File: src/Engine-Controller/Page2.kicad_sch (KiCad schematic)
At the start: 35 parts, among them P2 282837-6, P4 Micro_SD_Card, P5 USB, P6 140-504-415-000, P9 54602-908LF, Q1 QS5U17TR, U11 TS391IYLT, U4 SST25VF040B-50-4I-S2AE-T, U5 CP2102-GMR(QFN28), U7 SN65HVD71DR

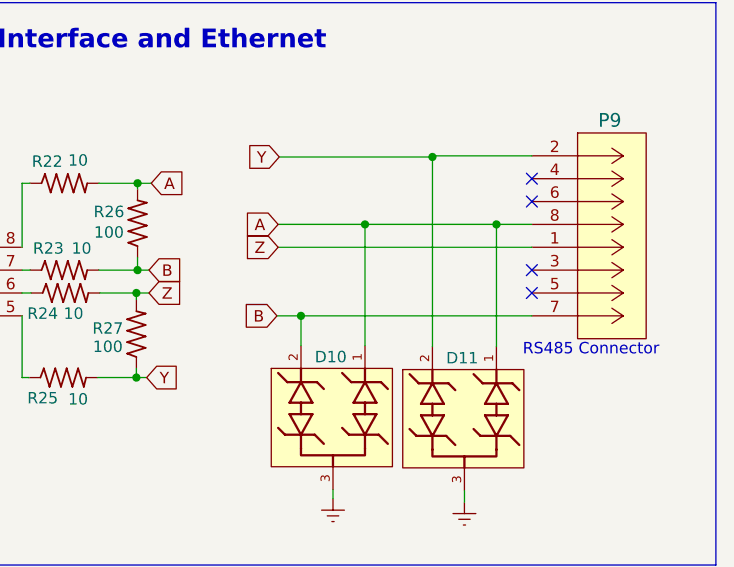
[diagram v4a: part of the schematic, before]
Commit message: fixed broken paths to step files and placed all 5.1 components on board
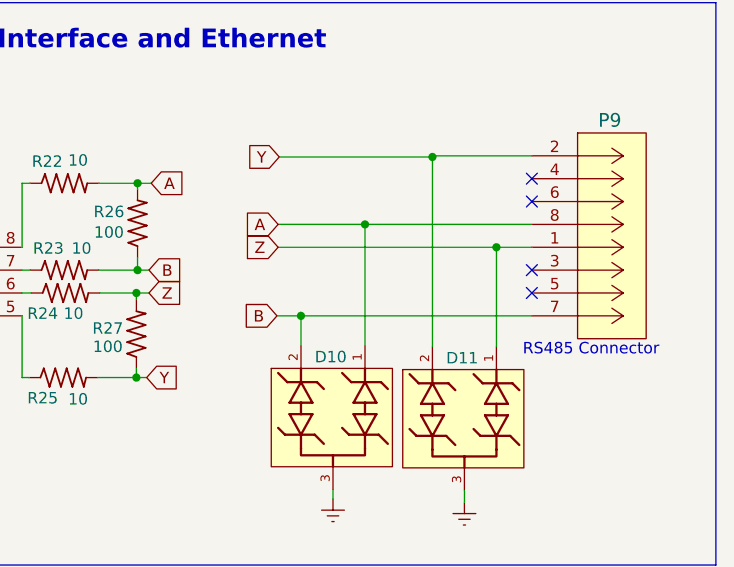
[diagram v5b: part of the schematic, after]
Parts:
- R22, R23, R24, R25, R26, R27: footprint (none) -> Engine-Controller:RES_0603
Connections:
- net A: no longer D11.1
- net Z: now also D11.1
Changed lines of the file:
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@@
   (junction (at 152.146 78.74) (diameter 0) (color 0 0 0 0)
   )
+  (junction (at 257.175 128.524) (diameter 0) (color 0 0 0 0)
+  )
   (junction (at 58.801 137.287) (diameter 0) (color 0 0 0 0)
   )
   (junction (at 144.272 66.04) (diameter 0) (color 0 0 0 0)
-  )
-  (junction (at 257.175 125.984) (diameter 0) (color 0 0 0 0)
   )
   (junction (at 113.792 132.969) (diameter 0) (color 0 0 0 0)
@@
     (stroke (width 0) (type default))
   )
-  (wire (pts (xy 242.57 125.984) (xy 257.175 125.984))
-    (stroke (width 0) (type default))
-  )
   (wire (pts (xy 217.297 131.064) (xy 218.567 131.064))
     (stroke (width 0) (type default))
@@
     (stroke (width 0) (type default))
   )
-  (wire (pts (xy 257.175 139.573) (xy 257.175 125.984))
-    (stroke (width 0) (type default))
-  )
   (wire (pts (xy 37.338 167.894) (xy 37.338 169.799))
     (stroke (width 0) (type default))
@@
     (stroke (width 0) (type default))
   )
+  (wire (pts (xy 257.175 128.524) (xy 232.918 128.524))
+    (stroke (width 0) (type default))
+  )
   (wire (pts (xy 24.13 124.587) (xy 24.892 124.587))
     (stroke (width 0) (type default))
@@
     (stroke (width 0) (type default))
   )
+  (wire (pts (xy 257.175 128.524) (xy 257.175 139.573))
+    (stroke (width 0) (type default))
+  )
   (wire (pts (xy 240.665 78.74) (xy 240.665 81.28))
     (stroke (width 0) (type default))
@@
     (stroke (width 0) (type default))
   )
-  (wire (pts (xy 257.175 125.984) (xy 261.112 125.984))
+  (wire (pts (xy 242.57 125.984) (xy 261.112 125.984))
     (stroke (width 0) (type default))
   )
@@
     (stroke (width 0) (type default))
   )
-  (wire (pts (xy 261.112 128.524) (xy 232.918 128.524))
+  (wire (pts (xy 261.112 128.524) (xy 257.175 128.524))
     (stroke (width 0) (type default))
   )
@@
       (effects (font (size 1.27 1.27)))
     )
-    (property "Footprint" "" (at 229.997 124.587 0)
+    (property "Footprint" "Engine-Controller:RES_0603" (at 229.997 124.587 0)
       (effects (font (size 1.27 1.27)) (justify left bottom) hide)
     )
@@
       (effects (font (size 1.27 1.27)))
     )
-    (property "Footprint" "" (at 210.312 155.702 0)
+    (property "Footprint" "Engine-Controller:RES_0603" (at 210.312 155.702 0)
       (effects (font (size 1.27 1.27)) (justify left bottom) hide)
     )
@@
       (effects (font (size 1.27 1.27)))
     )
-    (property "Footprint" "" (at 210.439 134.112 0)
+    (property "Footprint" "Engine-Controller:RES_0603" (at 210.439 134.112 0)
       (effects (font (size 1.27 1.27)) (justify left bottom) hide)
     )
@@
       (effects (font (size 1.27 1.27)))
     )
-    (property "Footprint" "" (at 210.566 146.304 0)
+    (property "Footprint" "Engine-Controller:RES_0603" (at 210.566 146.304 0)
       (effects (font (size 1.27 1.27)) (justify left bottom) hide)
     )
@@
       (effects (font (size 1.27 1.27)))
     )
-    (property "Footprint" "" (at 229.87 136.906 0)
+    (property "Footprint" "Engine-Controller:RES_0603" (at 229.87 136.906 0)
       (effects (font (size 1.27 1.27)) (justify left bottom) hide)
     )
@@
       (effects (font (size 1.27 1.27)))
     )
-    (property "Footprint" "" (at 210.439 143.764 0)
-      (effects (font (size 1.27 1.27)) (justify left bottom) hide)
-    )
+    (property "Footprint" "Engine-Controller:RES_0603" (at 210.439 143.764 0)
+      (effects (font (size 1.27 1.27)) (justify left bottom) hide)
+    )
